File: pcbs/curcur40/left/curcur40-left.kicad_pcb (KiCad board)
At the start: 2 copper layers, 124.3 x 91.8 mm, 79 parts, among them J1 TYPE-C-31-M-13C, J2 TRS, J4 Conn_01x03, SW1 SW_Push, SW10 SW_Push, SW11 SW_Push, SW12 SW_Push, SW13 SW_Push, SW14 SW_Push, SW15 SW_Push, SW16 SW_Push, SW17 SW_Push, SW18 SW_Push, SW2 SW_Push, SW3 SW_Push, SW4 SW_Push, SW5 SW_Push, SW6 SW_Push, SW7 SW_Push, SW8 SW_Push, SW9 SW_Push, U1 RP2040, U2 NCP1117LPST33T3G, U3 TPD4E05U06DQAR, U4 W25Q128JVSIQ, Y1 12MHz 18pF

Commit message: Unify SW1/rSW1 to 1u Choc footprint and document curcur40 component specs and sourcing in pcb_spec.md
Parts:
- SW1: footprint kbd:keyswitch_choc12_hotswap_1.5u -> kbd:keyswitch_choc12_hotswap_1u
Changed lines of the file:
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@@
 		)
 	)
-	(footprint "kbd:keyswitch_choc12_hotswap_1.5u"
+	(footprint "kbd:keyswitch_choc12_hotswap_1u"
 		(layer "B.Cu")
 		(at -33.3375 52.3875 180)
@@
 		)
 		(fp_line
-			(start 14.2875 9.525)
-			(end -14.2875 9.525)
+			(start 9.525 9.525)
+			(end -9.525 9.525)
 			(stroke
 				(width 0.1)
@@
 		)
 		(fp_line
-			(start 14.2875 -9.525)
-			(end 14.2875 9.525)
+			(start 9.525 -9.525)
+			(end 9.525 9.525)
 			(stroke
 				(width 0.1)
@@
 		)
 		(fp_line
-			(start -14.2875 9.525)
-			(end -14.2875 -9.525)
+			(start -9.525 9.525)
+			(end -9.525 -9.525)
 			(stroke
 				(width 0.1)
@@
 		)
 		(fp_line
-			(start -14.2875 -9.525)
-			(end 14.2875 -9.525)
+			(start -9.525 -9.525)
+			(end 9.525 -9.525)
 			(stroke
 				(width 0.1)

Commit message: Fix global pad_to_mask_clearance to 0mm, remove footprint solder_mask_margin overrides, and fix custom 3D model paths
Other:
- rule pad_to_mask_clearance: 0.2 -> 0

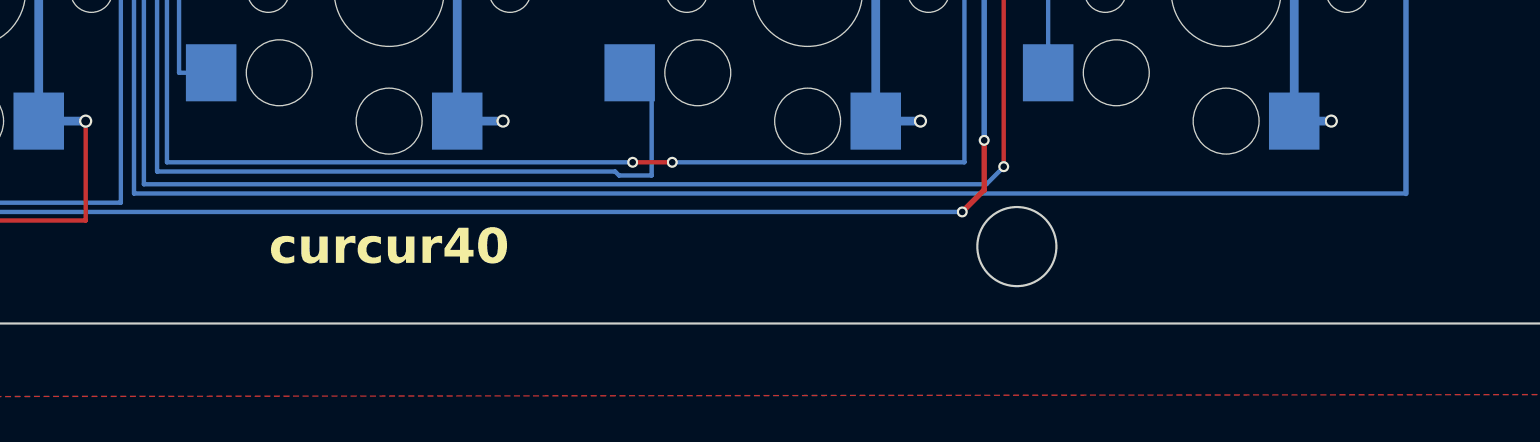
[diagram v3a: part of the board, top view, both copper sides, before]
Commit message: feat(mech): align left thumb mounting hole L5 (-21.5250, 63.6875) symmetrically with right TB4
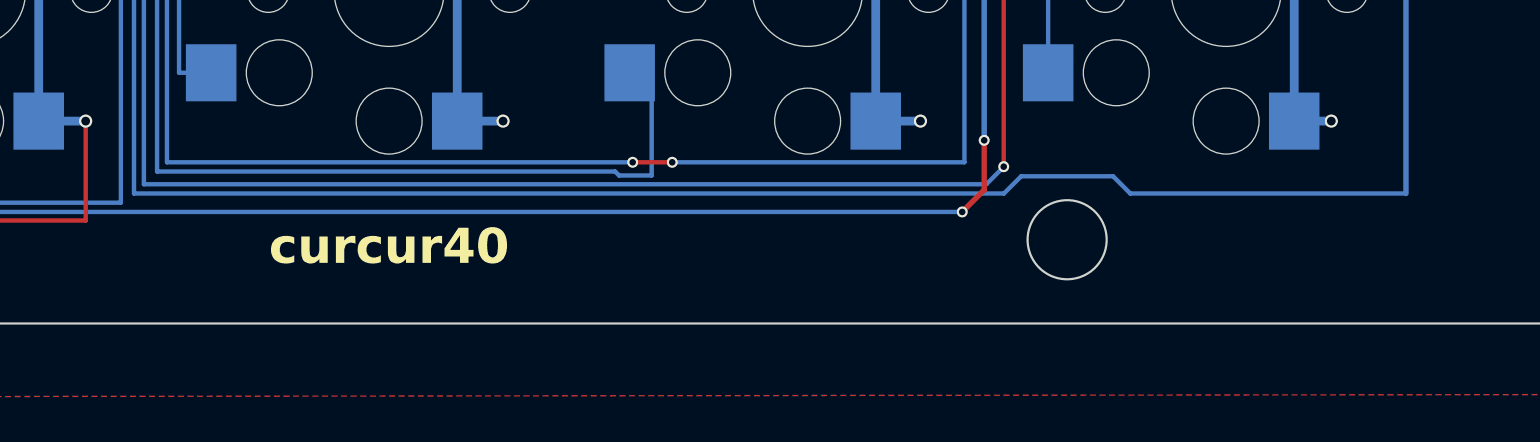
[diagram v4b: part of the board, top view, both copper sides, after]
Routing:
- net /TX: track 140.4 -> 141.1 mm
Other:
- outline, holes or cut-outs redrawn
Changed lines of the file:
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@@
 	)
 	(gr_circle
-		(center -23.8125 64)
-		(end -22.0125 64)
+		(center -21.525 63.6875)
+		(end -19.724999 63.6875)
 		(stroke
 			(width 0.1)
@@
 	)
 	(segment
-		(start -0.7425 29)
-		(end -10 29)
-		(width 0.25)
+		(start -24.4 61.5825)
+		(end -23.6175 60.8)
+		(width 0.2)
 		(layer "B.Cu")
 		(net "/TX")
 	)
 	(segment
-		(start -64 61.5825)
-		(end -6.1 61.5825)
-		(width 0.2)
+		(start -0.7425 29)
+		(end -10 29)
+		(width 0.25)
 		(layer "B.Cu")
 		(net "/TX")
@@
 	)
 	(segment
+		(start -19.4325 60.8)
+		(end -18.65 61.5825)
+		(width 0.2)
+		(layer "B.Cu")
+		(net "/TX")
+	)
+	(segment
 		(start -6.1 40)
 		(end -6.1 61.5825)
@@
 	)
 	(segment
+		(start -23.6175 60.8)
+		(end -19.4325 60.8)
+		(width 0.2)
+		(layer "B.Cu")
+		(net "/TX")
+	)
+	(segment
 		(start -71.5075 42.08)
 		(end -67.29 42.08)
@@
 	)
 	(segment
+		(start -64 61.5825)
+		(end -24.4 61.5825)
+		(width 0.2)
+		(layer "B.Cu")
+		(net "/TX")
+	)
+	(segment
 		(start -10 40)
 		(end -6.1 40)
@@
 		(width 0.2)
 		(layer "B.Cu")
+		(net "/TX")
+	)
+	(segment
+		(start -18.65 61.5825)
+		(end -6.1 61.5825)
+		(width 0.2)
+		(layer "B.Cu")
